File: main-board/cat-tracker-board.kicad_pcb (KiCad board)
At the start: 2 copper layers, 15.2 x 10.2 mm, 38 parts, among them J1 Conn_01x10, J2 USB_C_Receptacle_USB2.0, J3 Conn_01x03, Q1 SI3443DDV-T1-GE3, Q2 Q_PNP_BCE, Q3 Q_NPN_BCE, Q4 SI3443DDV-T1-GE3, Q5 SI3443DDV-T1-GE3, U1 ATSAMD21E18A-A, U2 LM3480-3.3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

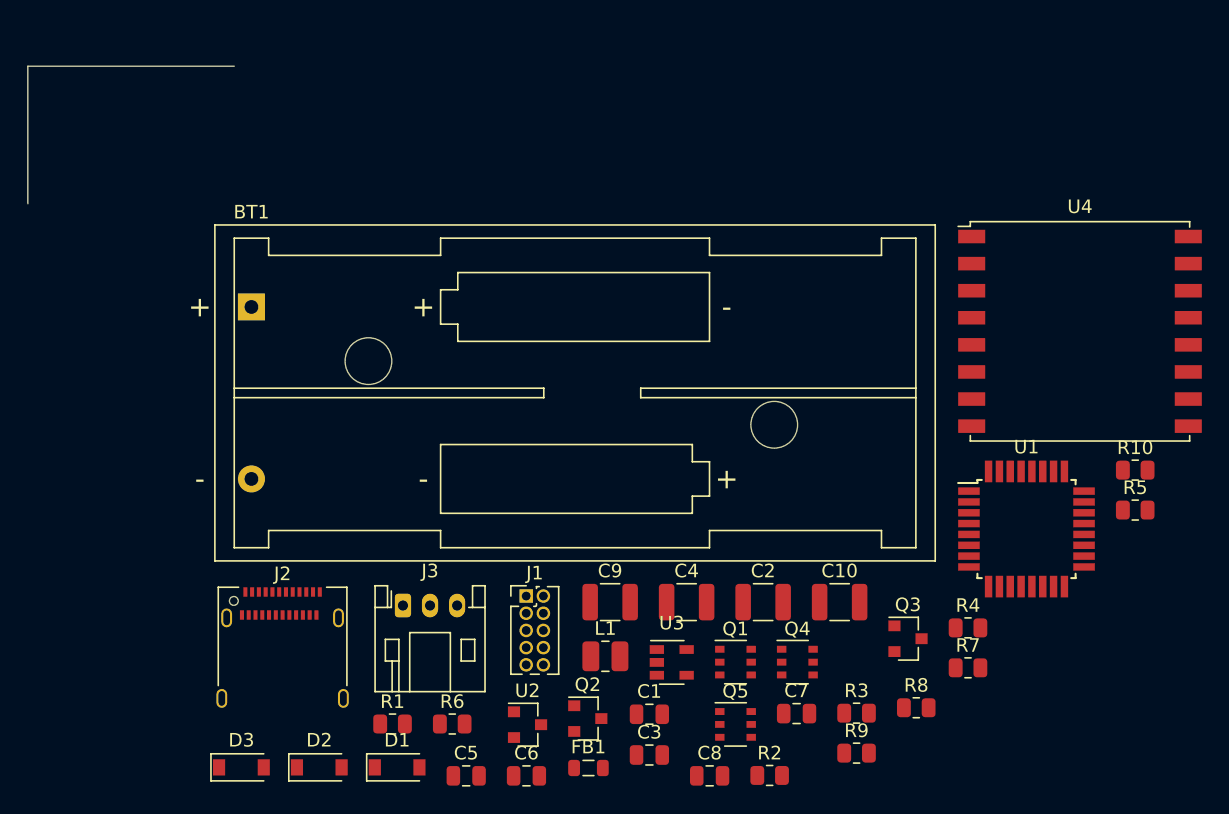
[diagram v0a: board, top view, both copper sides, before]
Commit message: Updated main board layout with battery board footprint.
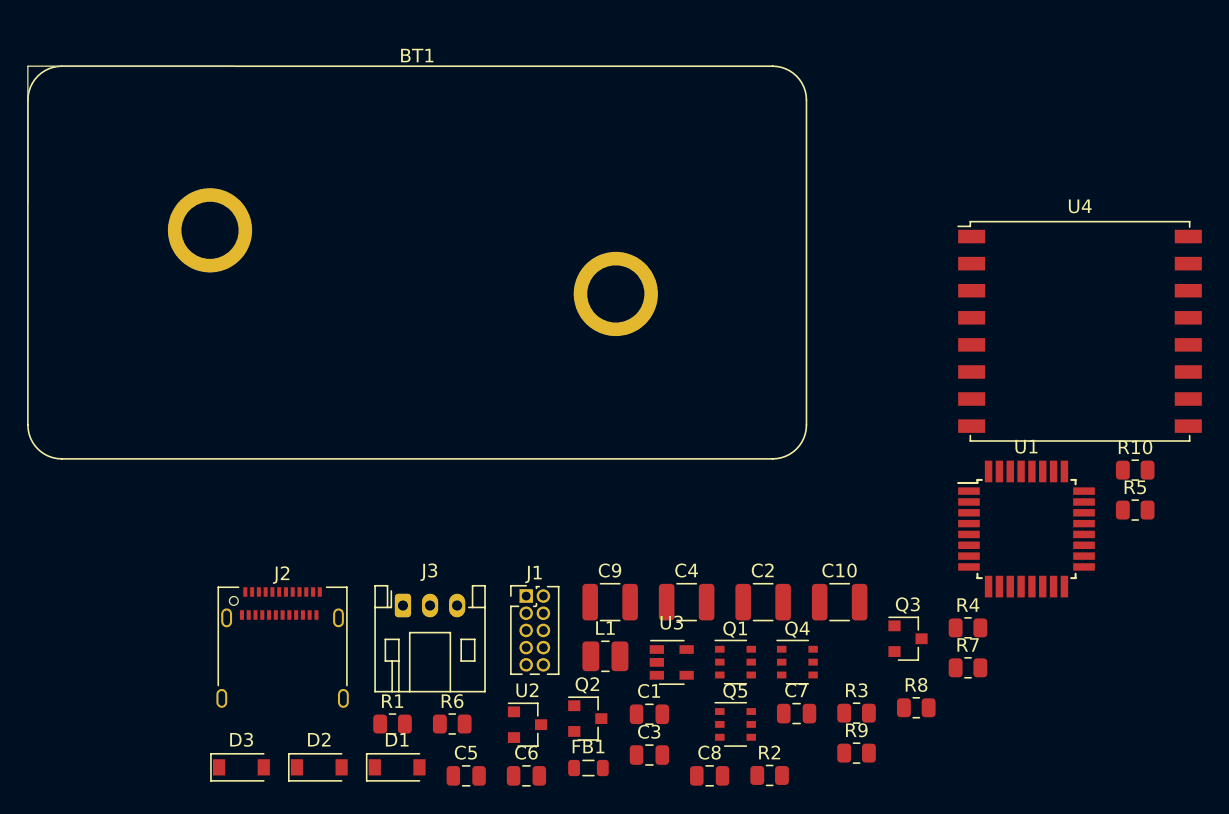
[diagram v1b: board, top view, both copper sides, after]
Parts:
- BT1: footprint Battery:BatteryHolder_Keystone_2468_2xAAA -> cat-tracker-board:battery-board
- moved BT1 12.7 mm to (28.8, 14.5)
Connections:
- J1 pad 6: Net-(J1-Pad6) -> (no net)
- J1 pad 7: Net-(J1-Pad7) -> (no net)
- J1 pad 8: Net-(J1-Pad8) -> (no net)
- J1 pad 9: Net-(J1-Pad9) -> (no net)
- J2 pad A8: Net-(J2-PadA8) -> (no net)
- J2 pad B8: Net-(J2-PadB8) -> (no net)
- U1 pad 1: Net-(U1-Pad1) -> (no net)
- U1 pad 15: Net-(U1-Pad15) -> (no net)
- U1 pad 16: Net-(U1-Pad16) -> (no net)
- U1 pad 19: Net-(U1-Pad19) -> (no net)
- U1 pad 2: Net-(U1-Pad2) -> (no net)
- U1 pad 20: Net-(U1-Pad20) -> (no net)
- U1 pad 21: Net-(U1-Pad21) -> (no net)
- U1 pad 22: Net-(U1-Pad22) -> (no net)
- U1 pad 25: Net-(U1-Pad25) -> (no net)
- U1 pad 27: Net-(U1-Pad27) -> (no net)
- U1 pad 5: Net-(U1-Pad5) -> (no net)
- U1 pad 6: Net-(U1-Pad6) -> (no net)
- U1 pad 7: Net-(U1-Pad7) -> (no net)
- U1 pad 8: Net-(U1-Pad8) -> (no net)
- U4 pad 11: Net-(U4-Pad11) -> (no net)
- U4 pad 12: Net-(U4-Pad12) -> (no net)
- U4 pad 15: Net-(U4-Pad15) -> (no net)
- U4 pad 16: Net-(U4-Pad16) -> (no net)
- U4 pad 7: Net-(U4-Pad7) -> (no net)
- U4 pad 9: Net-(U4-Pad9) -> (no net)

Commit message: Updated main board pcb.
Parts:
- added J4: Conn_01x02, cat-tracker-board:RF-Solutions-CON-SMA-EDGE-S, F.Cu at (65.0, 0.00)
- R6, R7: value 500k -> 510k
- moved U4 19.8 mm to (58.0, 17.8), turned to 90 degrees
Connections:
- U4 pad 9: (no net) -> Net-(J4-Pad1)
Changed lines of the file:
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@@
     (tracks 0)
     (zones 0)
-    (modules 38)
-    (nets 31)
+    (modules 39)
+    (nets 32)
   )
   (page A4)
@@
     (38 B.Mask user)
     (39 F.Mask user)
-    (40 Dwgs.User user hide)
+    (40 Dwgs.User user)
     (41 Cmts.User user hide)
     (42 Eco1.User user hide)
@@
     (pad_to_mask_clearance 0)
     (aux_axis_origin 0 0)
-    (visible_elements 7EFFFFFF)
+    (visible_elements 7EFFF7FF)
     (pcbplotparams
       (layerselection 0x010fc_ffffffff)
@@
   (net 29 /RFM_RESET)
   (net 30 /RFM_INT)
+  (net 31 "Net-(J4-Pad1)")
   (net_class Default "This is the default net class."
     (clearance 0.2)
@@
     (add_net "Net-(J2-PadB5)")
     (add_net "Net-(J2-PadB8)")
+    (add_net "Net-(J4-Pad1)")
     (add_net "Net-(L1-Pad1)")
     (add_net "Net-(Q2-Pad1)")
@@
     (add_net "Net-(U4-Pad16)")
     (add_net "Net-(U4-Pad7)")
-    (add_net "Net-(U4-Pad9)")
+  )
+  (module cat-tracker-board:RF-Solutions-CON-SMA-EDGE-S (layer F.Cu)
+    (at 65 0)
+    (fp_text reference J4 (at -6 2) (layer F.SilkS)
+      (effects (font (size 1 1) (thickness 0.15)))
+    )
+    (fp_text value Conn_01x02 (at 0 5.5) (layer F.Fab)
+      (effects (font (size 1 1) (thickness 0.15)))
+    )
+    (fp_line (start 3.25 4) (end 3.25 -9.5) (layer Dwgs.User) (width 0.12))
+    (fp_line (start 3.25 -9.5) (end -3.25 -9.5) (layer Dwgs.User) (width 0.12))
+    (fp_line (start -3.25 -9.5) (end -3.25 4) (layer Dwgs.User) (width 0.12))
+    (fp_line (start -3.25 4) (end -1.75 4) (layer Dwgs.User) (width 0.12))
+    (fp_line (start -1.75 4) (end -1.75 0) (layer Dwgs.User) (width 0.12))
+    (fp_line (start -1.75 0) (end -0.75 0) (layer Dwgs.User) (width 0.12))
+    (fp_line (start -0.75 0) (end -0.75 4) (layer Dwgs.User) (width 0.12))
+    (fp_line (start -0.75 4) (end 0.75 4) (layer Dwgs.User) (width 0.12))
+    (fp_line (start 0.75 4) (end 0.75 0) (layer Dwgs.User) (width 0.12))
+    (fp_line (start 0.75 0) (end 1.75 0) (layer Dwgs.User) (width 0.12))
+    (fp_line (start 1.75 0) (end 1.75 4) (layer Dwgs.User) (width 0.12))
+    (fp_line (start 1.75 4) (end 3.25 4) (layer Dwgs.User) (width 0.12))
+    (fp_line (start -3.25 0.25) (end -3.25 4.25) (layer F.SilkS) (width 0.12))
+    (fp_line (start -3.25 4.25) (end -1.75 4.25) (layer F.SilkS) (width 0.12))
+    (fp_line (start -1.75 4.25) (end -1.75 0.25) (layer F.SilkS) (width 0.12))
+    (fp_line (start -1.75 0.25) (end -0.75 0.25) (layer F.SilkS) (width 0.12))
+    (fp_line (start -0.75 0.25) (end -0.75 4.25) (layer F.SilkS) (width 0.12))
+    (fp_line (start -0.75 4.25) (end 0.75 4.25) (layer F.SilkS) (width 0.12))
+    (fp_line (start 0.75 4.25) (end 0.75 0.25) (layer F.SilkS) (width 0.12))
+    (fp_line (start 0.75 0.25) (end 1.75 0.25) (layer F.SilkS) (width 0.12))
+    (fp_line (start 1.75 0.25) (end 1.75 4.25) (layer F.SilkS) (width 0.12))
+    (fp_line (start 1.75 4.25) (end 3.25 4.25) (layer F.SilkS) (width 0.12))
+    (fp_line (start 3.25 4.25) (end 3.25 0.25) (layer F.SilkS) (width 0.12))
+    (fp_line (start 3.25 0.25) (end 3.75 0.25) (layer F.SilkS) (width 0.12))
+    (fp_line (start -3.25 0.25) (end -3.75 0.25) (layer F.SilkS) (width 0.12))
+    (fp_line (start 3.25 -8.75) (end -3.25 -7.25) (layer Dwgs.User) (width 0.12))
+    (fp_line (start 3.25 -7.75) (end -3.25 -6.25) (layer Dwgs.User) (width 0.12))
+    (fp_line (start 3.25 -6.75) (end -3.25 -5.25) (layer Dwgs.User) (width 0.12))
+    (fp_line (start 3.25 -5.75) (end -3.25 -4.25) (layer Dwgs.User) (width 0.12))
+    (fp_line (start 3.25 -4.75) (end -3.25 -3.25) (layer Dwgs.User) (width 0.12))
+    (pad 2 smd rect (at -2.5 2) (size 1.25 4) (layers B.Cu B.Paste B.Mask)
+      (net 1 /GND))
+    (pad 2 smd rect (at 2.5 2) (size 1.25 4) (layers B.Cu B.Paste B.Mask)
+      (net 1 /GND))
+    (pad 2 smd rect (at 2.5 2) (size 1.25 4) (layers F.Cu F.Paste F.Mask)
+      (net 1 /GND))
+    (pad 2 smd rect (at -2.5 2) (size 1.25 4) (layers F.Cu F.Paste F.Mask)
+      (net 1 /GND))
+    (pad 1 smd rect (at 0 2) (size 1.25 4) (layers F.Cu F.Paste F.Mask)
+      (net 31 "Net-(J4-Pad1)"))
   )
   (module cat-tracker-board:battery-board (layer F.Cu)
@@
   )
   (module RF_Module:HOPERF_RFM9XW_SMD (layer F.Cu)
-    (at 77.7 19.58)
+    (at 58 17.75 90)
     (descr "Low Power Long Range Transceiver Module SMD-16 (https://www.hoperf.com/data/upload/portal/20181127/5bfcbea20e9ef.pdf)")
     (tags "LoRa Low Power Long Range Transceiver Module")
     (attr smd)
-    (fp_text reference U4 (at 0 -9.2) (layer F.SilkS)
-      (effects (font (size 1 1) (thickness 0.15)))
-    )
-    (fp_text value RFM95W-915S2 (at 0 9.5) (layer F.Fab)
+    (fp_text reference U4 (at 0 -9.2 90) (layer F.SilkS)
+      (effects (font (size 1 1) (thickness 0.15)))
+    )
+    (fp_text value RFM95W-915S2 (at 0 9.5 90) (layer F.Fab)
       (effects (font (size 1 1) (thickness 0.15)))
     )
@@
     (fp_line (start 8 8) (end 8 -8) (layer F.Fab) (width 0.1))
     (fp_line (start -7 -8) (end 8 -8) (layer F.Fab) (width 0.1))
-    (fp_text user %R (at 0 0) (layer F.Fab)
-      (effects (font (size 1 1) (thickness 0.15)))
-    )
-    (pad 16 smd rect (at 8 -7) (size 2 1) (layers F.Cu F.Paste F.Mask))
-    (pad 15 smd rect (at 8 -5) (size 2 1) (layers F.Cu F.Paste F.Mask))
-    (pad 14 smd rect (at 8 -3) (size 2 1) (layers F.Cu F.Paste F.Mask)
+    (fp_text user %R (at 0 0 90) (layer F.Fab)
+      (effects (font (size 1 1) (thickness 0.15)))
+    )
+    (pad 16 smd rect (at 8 -7 90) (size 2 1) (layers F.Cu F.Paste F.Mask))
+    (pad 15 smd rect (at 8 -5 90) (size 2 1) (layers F.Cu F.Paste F.Mask))
+    (pad 14 smd rect (at 8 -3 90) (size 2 1) (layers F.Cu F.Paste F.Mask)
       (net 30 /RFM_INT))
-    (pad 13 smd rect (at 8 -1) (size 2 1) (layers F.Cu F.Paste F.Mask)
+    (pad 13 smd rect (at 8 -1 90) (size 2 1) (layers F.Cu F.Paste F.Mask)
       (net 4 /+3V3))
-    (pad 12 smd rect (at 8 1) (size 2 1) (layers F.Cu F.Paste F.Mask))
-    (pad 11 smd rect (at 8 3) (size 2 1) (layers F.Cu F.Paste F.Mask))
-    (pad 10 smd rect (at 8 5) (size 2 1) (layers F.Cu F.Paste F.Mask)
-      (net 1 /GND))
-    (pad 9 smd rect (at 8 7) (size 2 1) (layers F.Cu F.Paste F.Mask))
-    (pad 8 smd rect (at -8 7) (size 2 1) (layers F.Cu F.Paste F.Mask)
-      (net 1 /GND))
-    (pad 7 smd rect (at -8 5) (size 2 1) (layers F.Cu F.Paste F.Mask))
-    (pad 6 smd rect (at -8 3) (size 2 1) (layers F.Cu F.Paste F.Mask)
+    (pad 12 smd rect (at 8 1 90) (size 2 1) (layers F.Cu F.Paste F.Mask))
+    (pad 11 smd rect (at 8 3 90) (size 2 1) (layers F.Cu F.Paste F.Mask))
+    (pad 10 smd rect (at 8 5 90) (size 2 1) (layers F.Cu F.Paste F.Mask)
+      (net 1 /GND))
+    (pad 9 smd rect (at 8 7 90) (size 2 1) (layers F.Cu F.Paste F.Mask)
+      (net 31 "Net-(J4-Pad1)"))
+    (pad 8 smd rect (at -8 7 90) (size 2 1) (layers F.Cu F.Paste F.Mask)
+      (net 1 /GND))
+    (pad 7 smd rect (at -8 5 90) (size 2 1) (layers F.Cu F.Paste F.Mask))
+    (pad 6 smd rect (at -8 3 90) (size 2 1) (layers F.Cu F.Paste F.Mask)
       (net 29 /RFM_RESET))
-    (pad 5 smd rect (at -8 1) (size 2 1) (layers F.Cu F.Paste F.Mask)
+    (pad 5 smd rect (at -8 1 90) (size 2 1) (layers F.Cu F.Paste F.Mask)
       (net 26 /NSS))
-    (pad 4 smd rect (at -8 -1) (size 2 1) (layers F.Cu F.Paste F.Mask)
+    (pad 4 smd rect (at -8 -1 90) (size 2 1) (layers F.Cu F.Paste F.Mask)
       (net 27 /SCK))
-    (pad 3 smd rect (at -8 -3) (size 2 1) (layers F.Cu F.Paste F.Mask)
+    (pad 3 smd rect (at -8 -3 90) (size 2 1) (layers F.Cu F.Paste F.Mask)
       (net 28 /MOSI))
-    (pad 2 smd rect (at -8 -5) (size 2 1) (layers F.Cu F.Paste F.Mask)
+    (pad 2 smd rect (at -8 -5 90) (size 2 1) (layers F.Cu F.Paste F.Mask)
       (net 25 /MISO))
-    (pad 1 smd rect (at -8 -7) (size 2 1) (layers F.Cu F.Paste F.Mask)
+    (pad 1 smd rect (at -8 -7 90) (size 2 1) (layers F.Cu F.Paste F.Mask)
       (net 1 /GND))
     (model ${KISYS3DMOD}/RF_Module.3dshapes/HOPERF_RFM9XW_SMD.wrl
@@
       (effects (font (size 1 1) (thickness 0.15)))
     )
-    (fp_text value 500k (at 0 1.65) (layer F.Fab)
+    (fp_text value 510k (at 0 1.65) (layer F.Fab)
       (effects (font (size 1 1) (thickness 0.15)))
     )
@@
       (effects (font (size 1 1) (thickness 0.15)))
     )
-    (fp_text value 500k (at 0 1.65) (layer F.Fab)
-      (effects (font (size 1 1) (thickness 0.15)))
-    )
+    (fp_text value 510k (at 0 1.65) (layer F.Fab)
+      (effects (font (size 1 1) (thickness 0.15)))
+    )

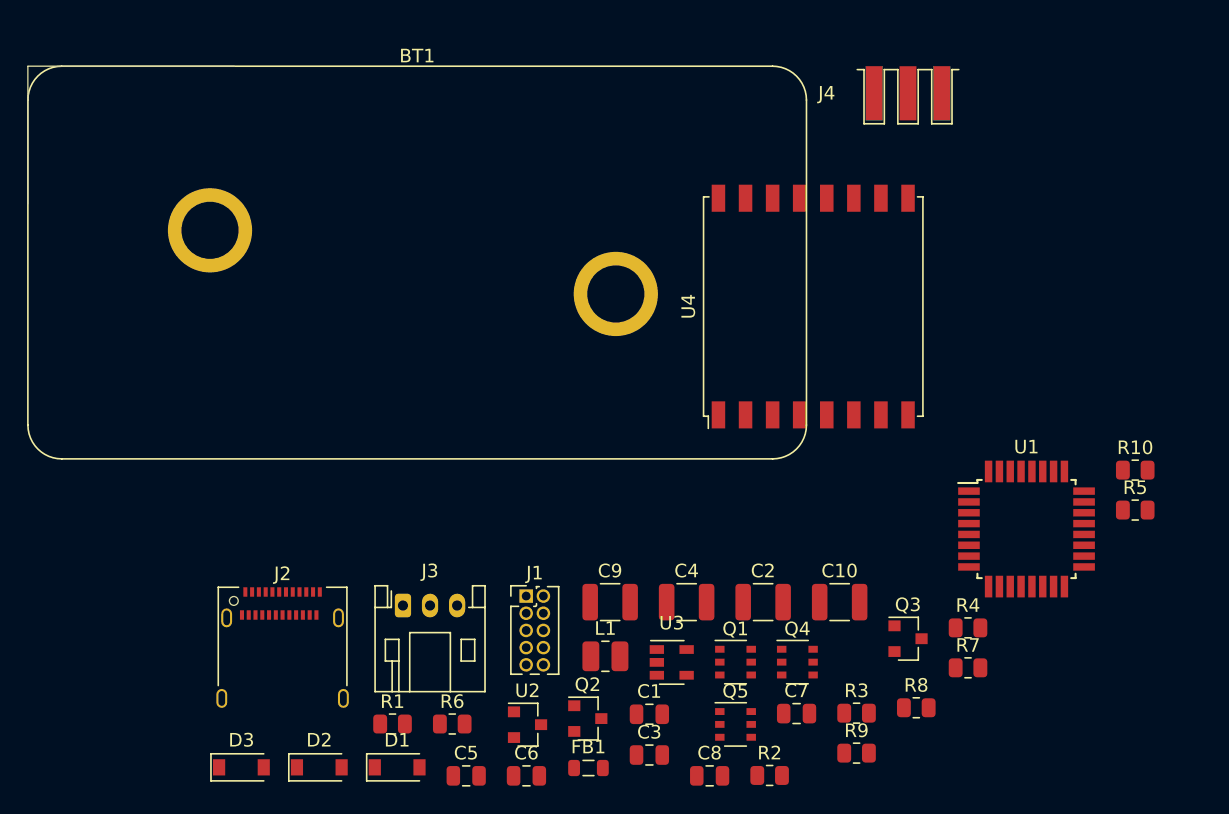
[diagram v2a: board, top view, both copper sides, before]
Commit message: Changed programming header to right angle and updated pcb.
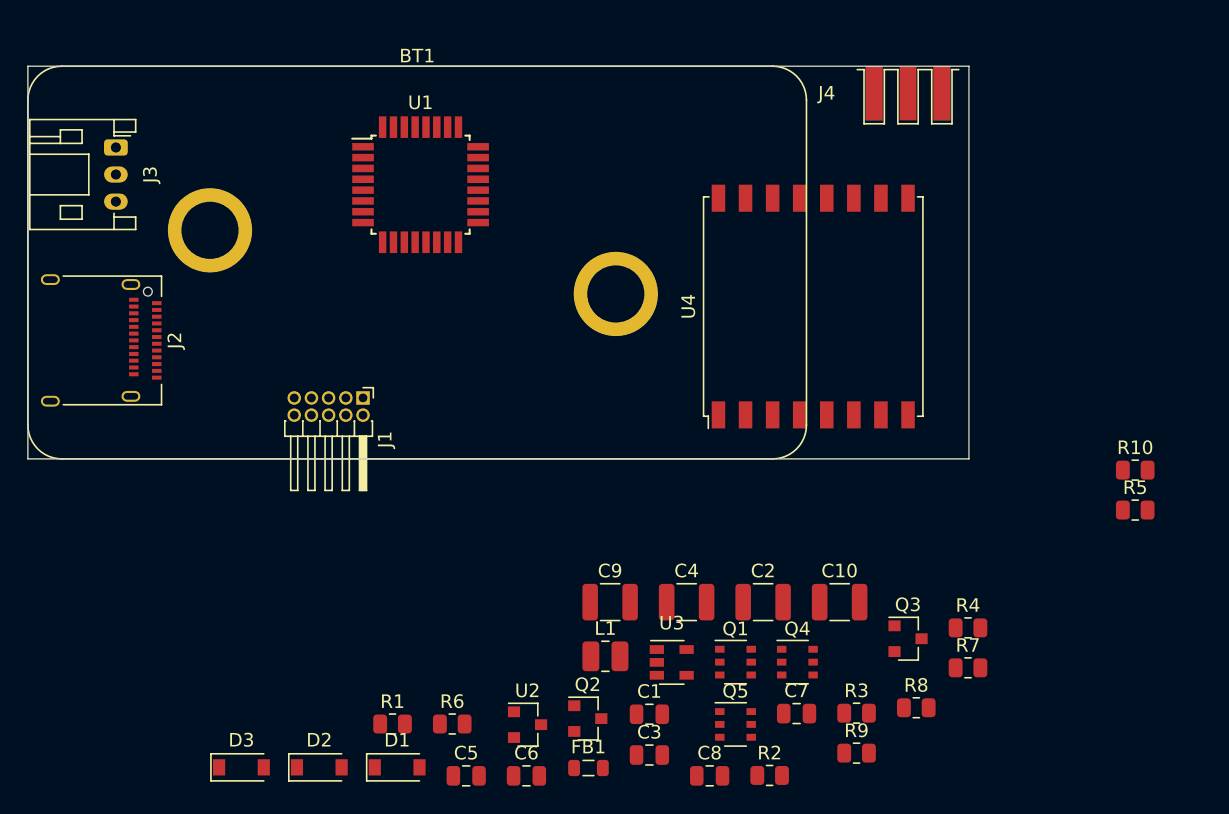
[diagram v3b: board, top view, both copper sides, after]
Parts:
- J1: footprint Connector_PinHeader_1.27mm:PinHeader_2x05_P1.27mm_Vertical -> Connector_PinHeader_1.27mm:PinHeader_2x05_P1.27mm_Horizontal
- moved U1 51.5 mm to (29.0, 8.75)
- moved J3 39.9 mm to (6.50, 6.00), turned to 270 degrees
- moved J2 27.6 mm to (4.50, 20.2), turned to 270 degrees
- moved J1 19.0 mm to (24.8, 24.5), turned to 270 degrees
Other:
- board size 15.2 x 10.2 mm -> 69.5 x 29 mm

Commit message: Placed all parts on board.
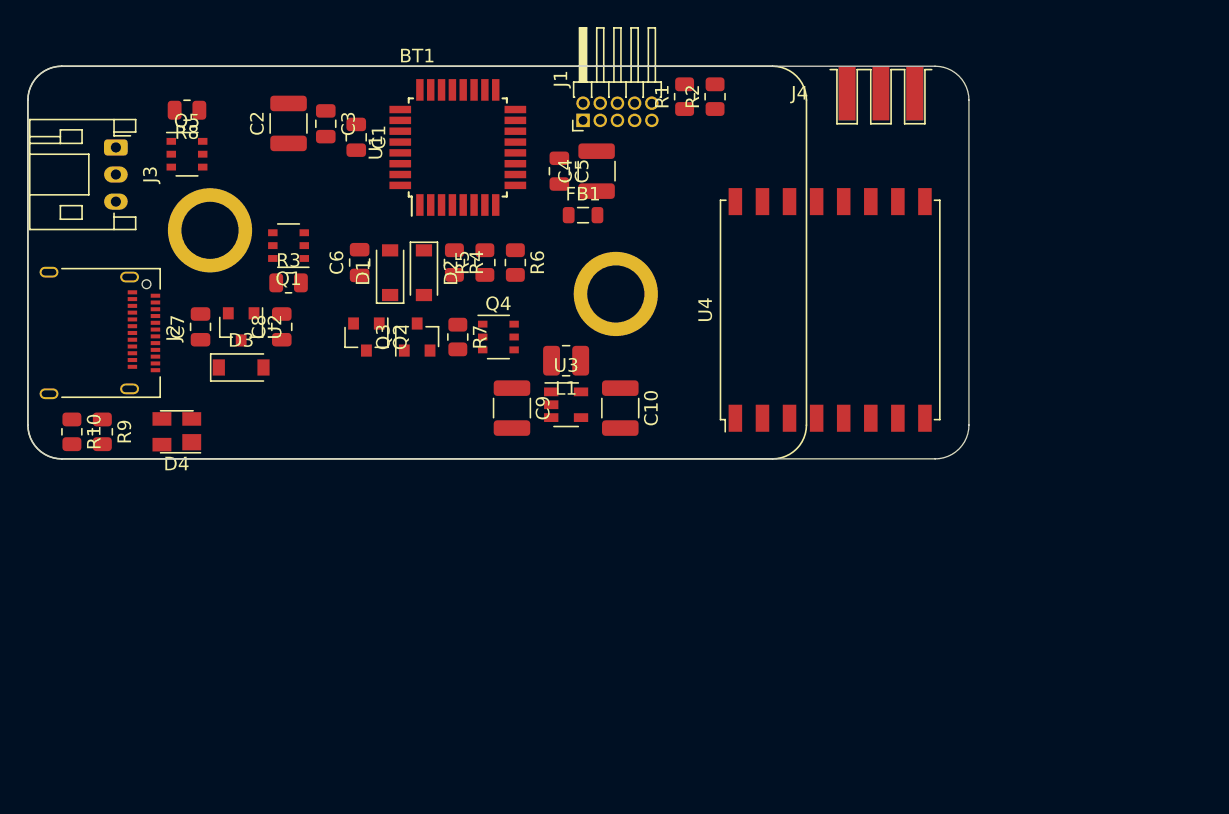
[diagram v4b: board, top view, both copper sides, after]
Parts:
- added D4: PRTR5V0U2X, Package_TO_SOT_SMD:SOT-143, F.Cu at (11.0, 27.0)
- moved R10 78.6 mm to (3.25, 27.0), turned to 270 degrees
- moved R8 69.6 mm to (11.8, 3.25), turned to 180 degrees
- moved R9 60.5 mm to (5.50, 27.0), turned to 270 degrees
- moved Q5 58.4 mm to (11.8, 6.50)
- moved R3 52.6 mm to (19.2, 16.0)
- moved C7 52.5 mm to (12.8, 19.2), turned to 90 degrees
- moved C3 52.4 mm to (22.0, 4.25), turned to 270 degrees
- moved R5 51.4 mm to (33.8, 14.5), turned to 90 degrees
- moved R1 51.1 mm to (48.5, 2.25), turned to 90 degrees
- moved R2 50.3 mm to (50.8, 2.25), turned to 90 degrees
- moved C2 49.8 mm to (19.2, 4.22), turned to 90 degrees
- moved C1 47.8 mm to (24.2, 5.25), turned to 270 degrees
- moved R4 46.5 mm to (31.5, 14.5), turned to 270 degrees
- moved C8 45.8 mm to (18.8, 19.2), turned to 90 degrees
- moved C5 45.2 mm to (39.2, 7.75), turned to 270 degrees
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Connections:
- U1 pad 15: (no net) -> /RFM_INT
- U1 pad 16: (no net) -> /RFM_RESET
- U1 pad 3: /RFM_INT -> (no net)
- U1 pad 4: /RFM_RESET -> (no net)
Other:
- outline, holes or cut-outs redrawn
